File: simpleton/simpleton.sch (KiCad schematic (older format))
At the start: 51 parts

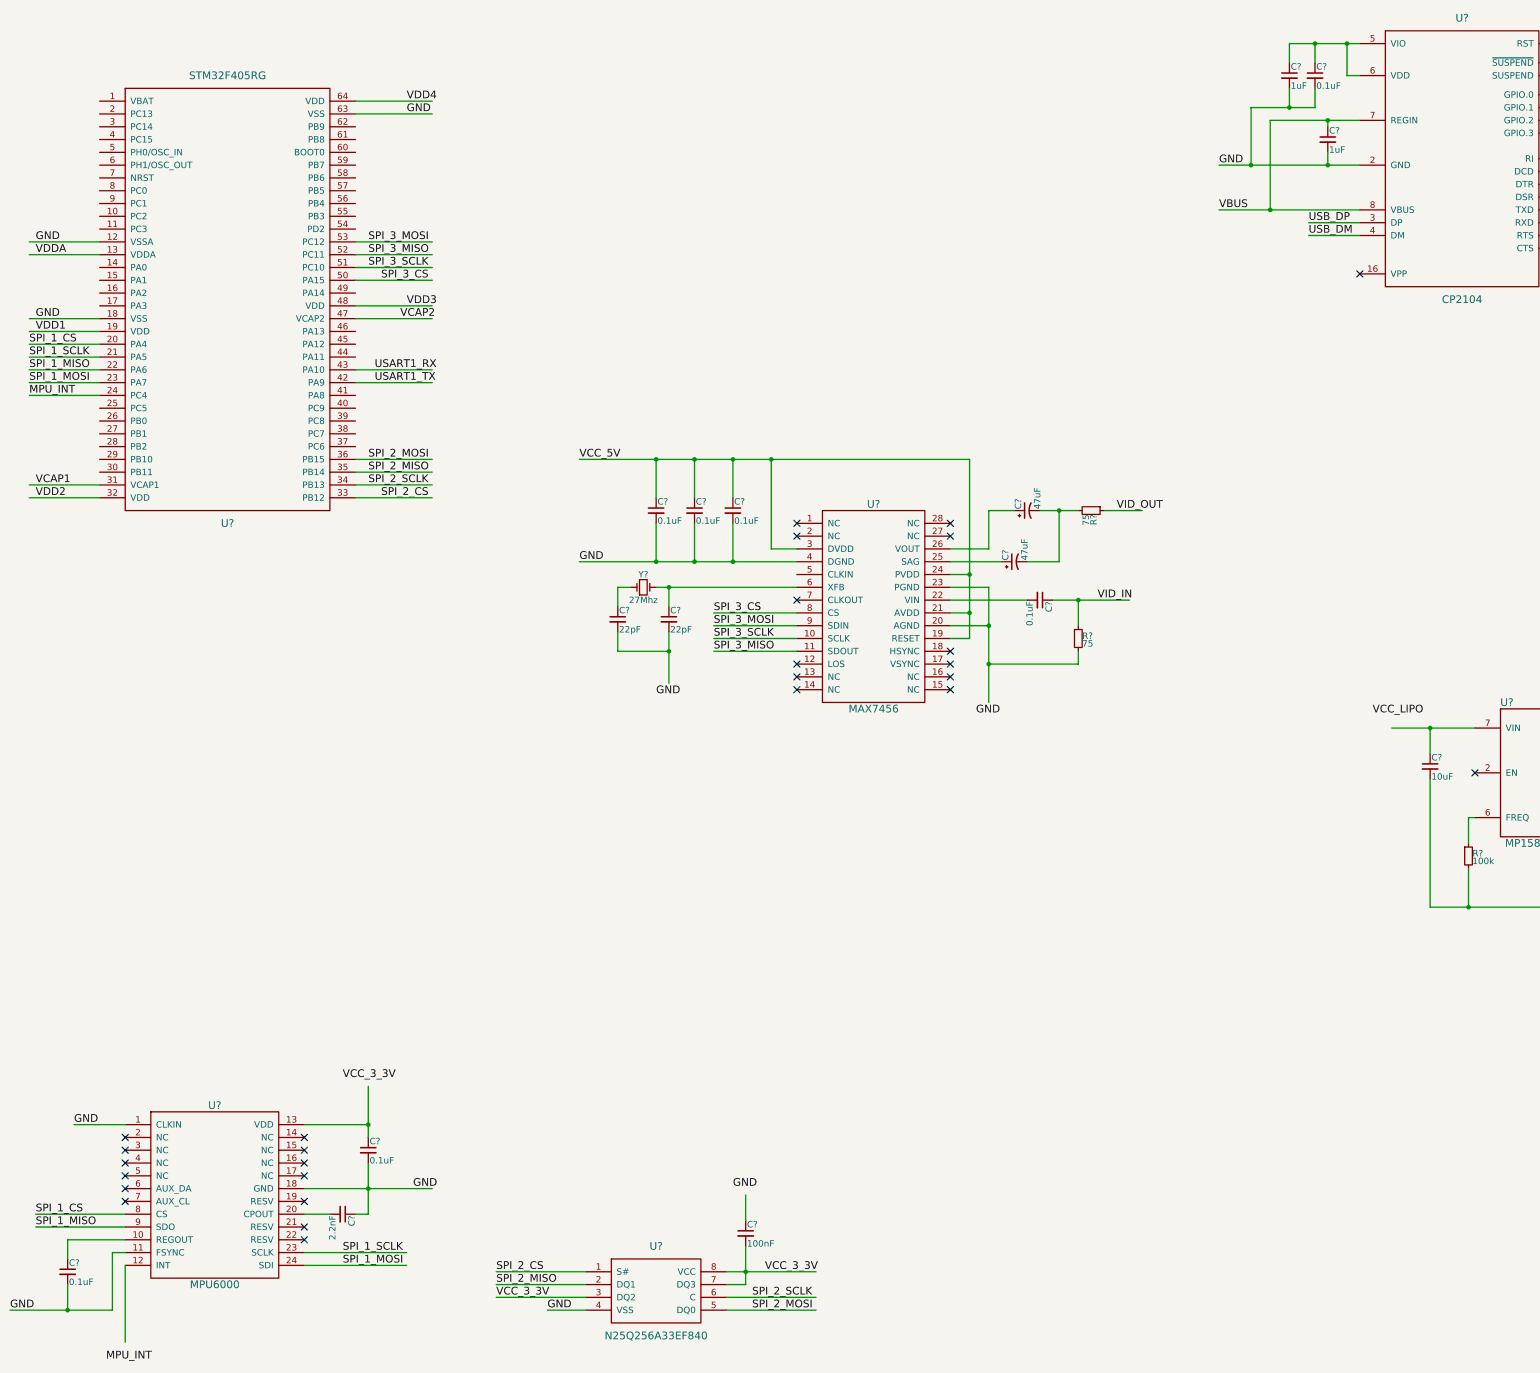
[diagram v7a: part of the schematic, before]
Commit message: Added UARTs and inverters
Closes #8

- Added SN74LVC2G86 data sheet
- Created SN74LVC2G86 component
- Wired up 3x SN74LVC2G86 (one for each UART) in the schematic
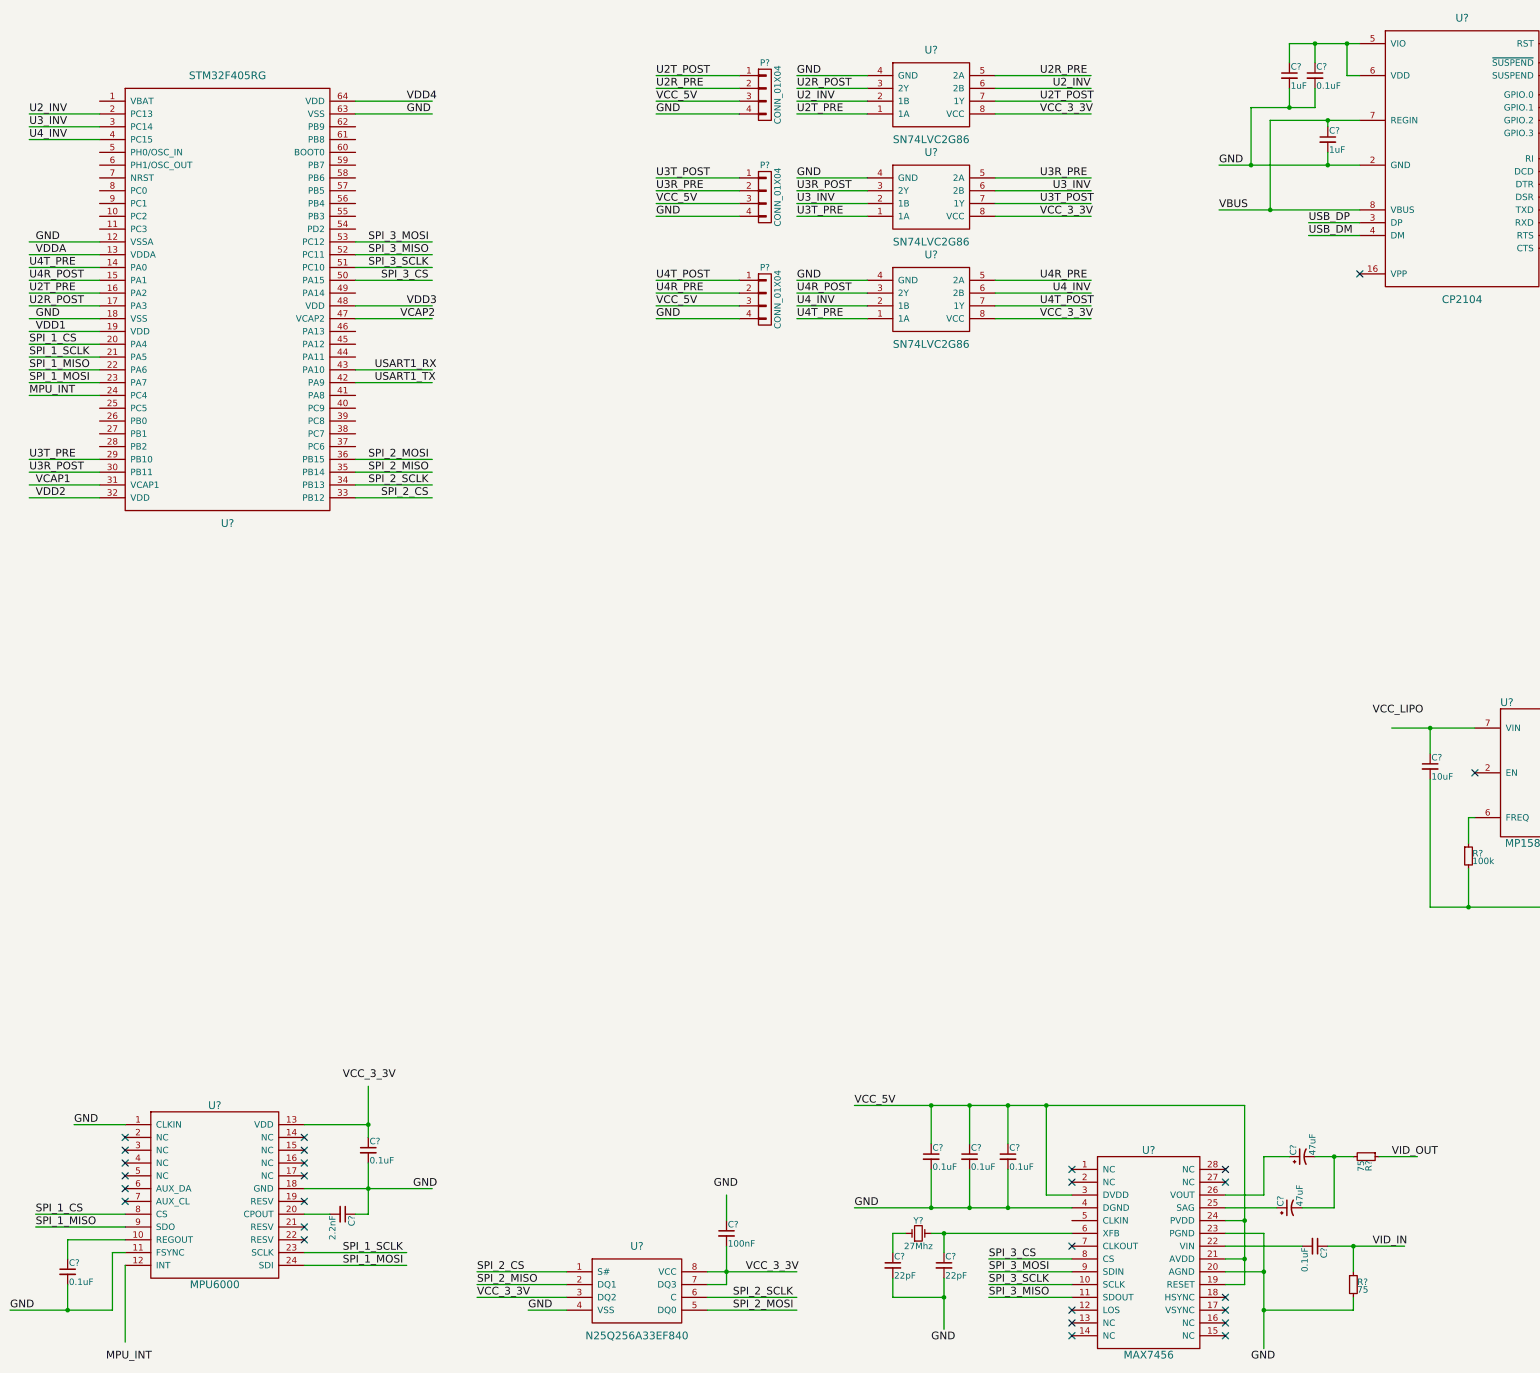
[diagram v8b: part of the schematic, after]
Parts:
- added P? (x3): CONN_01X04, symbol CONN_01X04
- added U? (x3): SN74LVC2G86, symbol SN74LVC2G86
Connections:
- net labels added: U2R_POST, U2R_PRE, U2T_POST, U2T_PRE, U2_INV, U3R_POST, U3R_PRE, U3T_POST, U3T_PRE, U3_INV, U4R_POST, U4R_PRE, U4T_POST, U4T_PRE, U4_INV
- wire segments 183 -> 228
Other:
- moved on the sheet: C?, R?, U?, Y?
